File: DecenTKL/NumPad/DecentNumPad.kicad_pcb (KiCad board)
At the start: 2 copper layers, 78.6 x 146.7 mm, 129 parts, among them J1 Joystick1, J2 Joystick2, J3 Conn_02x20_Counter_Clockwise, J4 USB_A, J5 USB_C_Receptacle_USB2.0_16P, J6 USB_A, J7 USB_A, SW1 BOOTSEL, SW10 SW_Push, SW11 SW_Push, SW12 SW_Push, SW13 SW_Push, SW14 SW_Push, SW15 SW_Push, SW16 SW_Push, SW17 SW_Push, SW18 SW_Push, SW19 SW_Push, SW2 SW_Push, SW20 SW_Push, SW3 SW_Push, SW4 SW_Push, SW5 SW_Push, SW6 SW_Push, SW7 SW_Push, SW8 SW_Push, SW9 SW_Push, U1 NCP1117-3.3_SOT223, U2 W25Q128JVS, U3 RP2040, U4 CH334R, U5 CH213, Y1 ABM8-272-T3

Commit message: DecenTKL numpad update
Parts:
- added G***: LOGO, LOGO, F.Cu at (80.0, 19.0)
- added G***: LOGO, LOGO, B.Cu at (74.8, 159.6)
- added G***: LOGO, Library:ScreamingAtTheRadio, B.Cu at (93.8, 155.9)
- added REF**: KiCad-Logo2_6mm_Copper, Symbol:KiCad-Logo2_6mm_Copper, B.Cu at (50.3, 157.6)
- added REF**: OSHW-Logo2_7.3x6mm_Copper, Symbol:OSHW-Logo2_7.3x6mm_Copper, B.Cu at (40.1, 158.7)
- C1, C10, C11, C12, C13, C14, C15, C16, C17, C18, C19, C2, C3, C36, C37, C38, C4, C5, C6, C7, C8, C9: value 104 -> 100nF
- J5: footprint Connector_USB:USB_C_Receptacle_HRO_TYPE-C-31-M-12 -> Connector_USB:USB_C_Receptacle_HCTL_HC-TYPE-C-16P-01A
- SW17, SW8: footprint DecenTKL:Kailh_socket_MX_1-00U -> DecenTKL:Kailh_socket_MX_2-00U_V
- SW19: footprint DecenTKL:Kailh_socket_MX_1-00U -> DecenTKL:Kailh_socket_MX_2-00U
- moved C37 18.1 mm to (42.7, 142.3)
- moved C38 17.8 mm to (90.4, 132.8), turned to 90 degrees
- moved C36 16.7 mm to (90.3, 94.7)
- moved C18 14.6 mm to (27.5, 145.1)
- moved D41 14.3 mm to (94.6, 134.3)
- moved D39 14.3 mm to (94.6, 96.2)
- moved C4 9.74 mm to (51.2, 67.4), turned to 180 degrees
- moved D40 9.54 mm to (47.0, 143.8)
- moved C7 9.51 mm to (89.6, 83.3), turned to 180 degrees
- moved C16 9.50 mm to (89.6, 121.5), turned to 180 degrees
- moved C5 9.43 mm to (70.5, 66.9), turned to 180 degrees
- moved C6 9.38 mm to (89.6, 66.9), turned to 180 degrees
- moved C15 8.59 mm to (71.3, 123.3)
- moved C12 8.59 mm to (71.3, 104.2)
- moved C3 8.59 mm to (33.2, 66.0)
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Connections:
- D10 pad 1: /Minus/RGB_IN -> VBUS
- D10 pad 2: GND -> /Minus/RGB_IN
- D10 pad 3: /Over/RGB_OUT -> GND
- D10 pad 4: VBUS -> /Over/RGB_OUT
- D12 pad 1: /Minus/RGB_OUT -> VBUS
- D12 pad 2: GND -> /Minus/RGB_OUT
- D12 pad 3: /Minus/RGB_IN -> GND
- D12 pad 4: VBUS -> /Minus/RGB_IN
- D14 pad 1: /Four/RGB_IN -> VBUS
- D14 pad 2: GND -> /Four/RGB_IN
- D14 pad 3: /Nine/RGB_OUT -> GND
- D14 pad 4: VBUS -> /Nine/RGB_OUT
- D16 pad 1: /Eight/RGB_IN -> VBUS
- D16 pad 2: GND -> /Eight/RGB_IN
- D16 pad 3: /Minus/RGB_OUT -> GND
- D16 pad 4: VBUS -> /Minus/RGB_OUT
- D18 pad 1: /Eight/RGB_OUT -> VBUS
- D18 pad 2: GND -> /Eight/RGB_OUT
- D18 pad 3: /Eight/RGB_IN -> GND
- D18 pad 4: VBUS -> /Eight/RGB_IN
- D2 pad 1: /F11/RGB_OUT -> VBUS
- D2 pad 2: GND -> /F11/RGB_OUT
- D2 pad 3: RGB -> GND
- D2 pad 4: VBUS -> RGB
- D20 pad 1: /Nine/RGB_OUT -> VBUS
- D20 pad 2: GND -> /Nine/RGB_OUT
- D20 pad 3: /Eight/RGB_OUT -> GND
- D20 pad 4: VBUS -> /Eight/RGB_OUT
- D22 pad 1: /Five/RGB_OUT -> VBUS
- D22 pad 2: GND -> /Five/RGB_OUT
- D22 pad 3: /Five/RGB_IN -> GND
- D22 pad 4: VBUS -> /Five/RGB_IN
- D24 pad 1: /RGB44/RGB_IN -> VBUS
- D24 pad 2: GND -> /RGB44/RGB_IN
- D24 pad 3: /Five/RGB_OUT -> GND
- D24 pad 4: VBUS -> /Five/RGB_OUT
- D26 pad 1: /Three/RGB_IN -> VBUS
- D26 pad 2: GND -> /Three/RGB_IN
- D26 pad 3: /One/RGB_OUT -> GND
- D26 pad 4: VBUS -> /One/RGB_OUT
- D28 pad 1: /Five/RGB_IN -> VBUS
- D28 pad 2: GND -> /Five/RGB_IN
- D28 pad 3: /Four/RGB_IN -> GND
- D28 pad 4: VBUS -> /Four/RGB_IN
- D30 pad 1: /Enter/RGB_IN -> VBUS
- D30 pad 2: GND -> /Enter/RGB_IN
- D30 pad 3: /Three/RGB_IN -> GND
- D30 pad 4: VBUS -> /Three/RGB_IN
- D32 pad 1: /Enter/RGB_OUT -> VBUS
- D32 pad 2: GND -> /Enter/RGB_OUT
- D32 pad 3: /Enter/RGB_IN -> GND
- D32 pad 4: VBUS -> /Enter/RGB_IN
- D34 pad 1: /One/RGB_OUT -> VBUS
- D34 pad 2: GND -> /One/RGB_OUT
- D34 pad 3: /One/RGB_IN -> GND
- D34 pad 4: VBUS -> /One/RGB_IN
- D36 pad 1: /RGB62/RGB_IN -> VBUS
- D36 pad 2: GND -> /RGB62/RGB_IN
- D36 pad 3: /Enter/RGB_OUT -> GND
- D36 pad 4: VBUS -> /Enter/RGB_OUT
- D38 pad 1: /Point/RGB_OUT -> VBUS
- D38 pad 2: GND -> /Point/RGB_OUT
- D38 pad 3: /Point/RGB_IN -> GND
- D38 pad 4: VBUS -> /Point/RGB_IN
- D39 pad 1: /One/RGB_IN -> VBUS
- D39 pad 2: GND -> /One/RGB_IN
- D39 pad 3: /RGB44/RGB_IN -> GND
- D39 pad 4: VBUS -> /RGB44/RGB_IN
- D4 pad 1: /F12/RGB_OUT -> VBUS
- D4 pad 2: GND -> /F12/RGB_OUT
- D4 pad 3: /F11/RGB_OUT -> GND
- D4 pad 4: VBUS -> /F11/RGB_OUT
- D40 pad 1: /Point/RGB_IN -> VBUS
- D40 pad 2: GND -> /Point/RGB_IN
- D40 pad 3: /RGB62/RGB_IN -> GND
- D40 pad 4: VBUS -> /RGB62/RGB_IN
- D41 pad 1: /RGB63/RGB_OUT -> VBUS
- D41 pad 2: GND -> /RGB63/RGB_OUT
- D41 pad 3: /Point/RGB_OUT -> GND
- D41 pad 4: VBUS -> /Point/RGB_OUT
- D6 pad 1: /Num/RGB_OUT -> VBUS
- D6 pad 2: GND -> /Num/RGB_OUT
- D6 pad 3: /F12/RGB_OUT -> GND
- D6 pad 4: VBUS -> /F12/RGB_OUT
- D8 pad 1: /Over/RGB_OUT -> VBUS
- D8 pad 2: GND -> /Over/RGB_OUT
- D8 pad 3: /Num/RGB_OUT -> GND
- D8 pad 4: VBUS -> /Num/RGB_OUT
- J4 pad 5: unconnected-(J4-Shield-Pad5)_1 -> GND
- J5 pad S1: unconnected-(J5-SHIELD-PadS1)_1 -> GND
- J6 pad 5: unconnected-(J6-Shield-Pad5)_1 -> GND
- J7 pad 5: unconnected-(J7-Shield-Pad5)_1 -> GND
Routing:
- net VBUS: track 608.6 -> 709.9 mm
- net /Point/RGB_IN: track 14.1 -> 38.6 mm
- net GND: track 95.6 -> 119.7 mm, vias 96 -> 98
- net Net-(U5-VI+): track 23.0 -> 46.5 mm
- net /Point/RGB_OUT: track 14.8 -> 37.7 mm
- net /F12/RGB_OUT: track 97.9 -> 75.6 mm
- net /RGB44/RGB_IN: track 14.8 -> 37.0 mm
- net /F11/RGB_OUT: track 24.2 -> 44.6 mm
- net /Nine/RGB_OUT: track 14.1 -> 31.7 mm
- net /Enter/RGB_IN: track 14.1 -> 31.5 mm
- net /Minus/RGB_IN: track 14.1 -> 30.5 mm
- net /Num/RGB_OUT: track 14.1 -> 29.3 mm
- net /Over/RGB_OUT: track 14.1 -> 29.2 mm
- net /Eight/RGB_IN: track 14.1 -> 29.1 mm
- net /Five/RGB_IN: track 14.1 -> 29.0 mm
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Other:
- board size 78.6 x 146.7 mm -> 80.6 x 146.7 mm
- board text added: "*"
- board text added: "+"
- board text added: "-"
- board text added: "."
- board text added: "/"
- board text added: "0"
- board text added: "1"
- board text added: "2"
- board text added: "3"
- board text added: "3.3V"
- board text added: "4"
- board text added: "5"
- board text added: "6"
- board text added: "7"
- board text added: "8"
- board text added: "9"
- board text added: "Boot select"
- board text added: "COL0"
- board text added: "COL1"
- board text added: "COL2"
- board text added: "COL3"
- board text added: "DecenTKL numpad © Bertrand Le Roy 2024"
- board text added: "DecenTKL numpad © Bertrand Le Roy 2024 github.com/bleroy/3d-junkyard/DecenTKL"
- board text added: "Enter"
- board text added: "F11"
- board text added: "F12"
- board text added: "GND"
- board text added: "GP21"
- board text added: "GP22"
- board text added: "Joy 1"
- board text added: "Joy 2"
- board text added: "Joy1 down"
- board text added: "Joy1 left"
- board text added: "Joy1 right"
- board text added: "Joy1 trigger"
- board text added: "Joy1 up"
- board text added: "Joy2 down"
- board text added: "Joy2 left"
- board text added: "Joy2 right"
- board text added: "Joy2 trigger"
- board text added: "Joy2 up"
- board text added: "Num"
- board text added: "Paddle 2A"
- board text added: "Paddle 2B"
- board text added: "RGB"
- board text added: "ROW0"
- board text added: "ROW1"
- board text added: "ROW2"
- board text added: "ROW3"
- board text added: "ROW4"
- board text added: "ROW5"
- board text added: "USB 1"
- board text added: "USB 2"
- board text added: "USB 3"
- board text added: "USB in"

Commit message: DecenTKL NumPad WIP
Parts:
- SW10, SW11, SW12, SW13, SW14, SW15, SW16, SW17, SW18, SW19, SW2, SW20, SW3, SW4, SW5, SW6, SW7, SW8, SW9: value SW_Push -> MX
- moved J2 0.79 mm to (95.6, 42.1)
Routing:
- net JOY2_PADDLEA: track 106.5 -> 112.0 mm
- net JOY2_UP: track 73.1 -> 77.7 mm
- net JOY2_PADDLEB: track 94.7 -> 97.4 mm
- net JOY2_RIGHT: track 119.8 -> 121.4 mm
- net GP22: track 100.8 -> 102.0 mm
- net /2040/USB_BOOT: track 188.6 -> 189.6 mm
- net RGB: track 101.0 -> 102.0 mm
- net GP21: track 94.3 -> 95.2 mm
- net JOY2_LEFT: track 93.2 -> 94.1 mm
- net JOY2_DOWN: track 91.3 -> 90.5 mm
- net JOY2_TRIGGER: track 128.3 -> 129.0 mm
- net GND: track 119.7 -> 120.0 mm, vias 98 -> 100

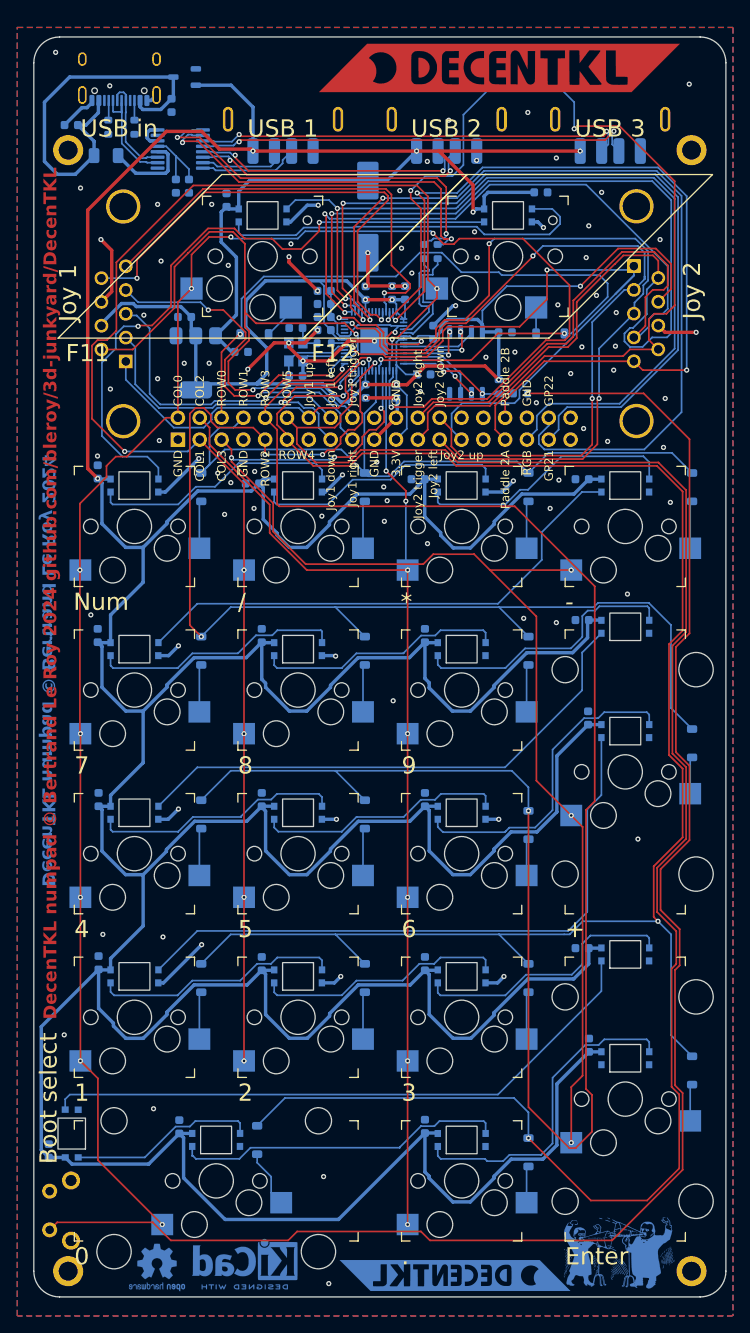
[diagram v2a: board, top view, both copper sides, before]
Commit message: DecenTKL NumPad rev. 1 finalized
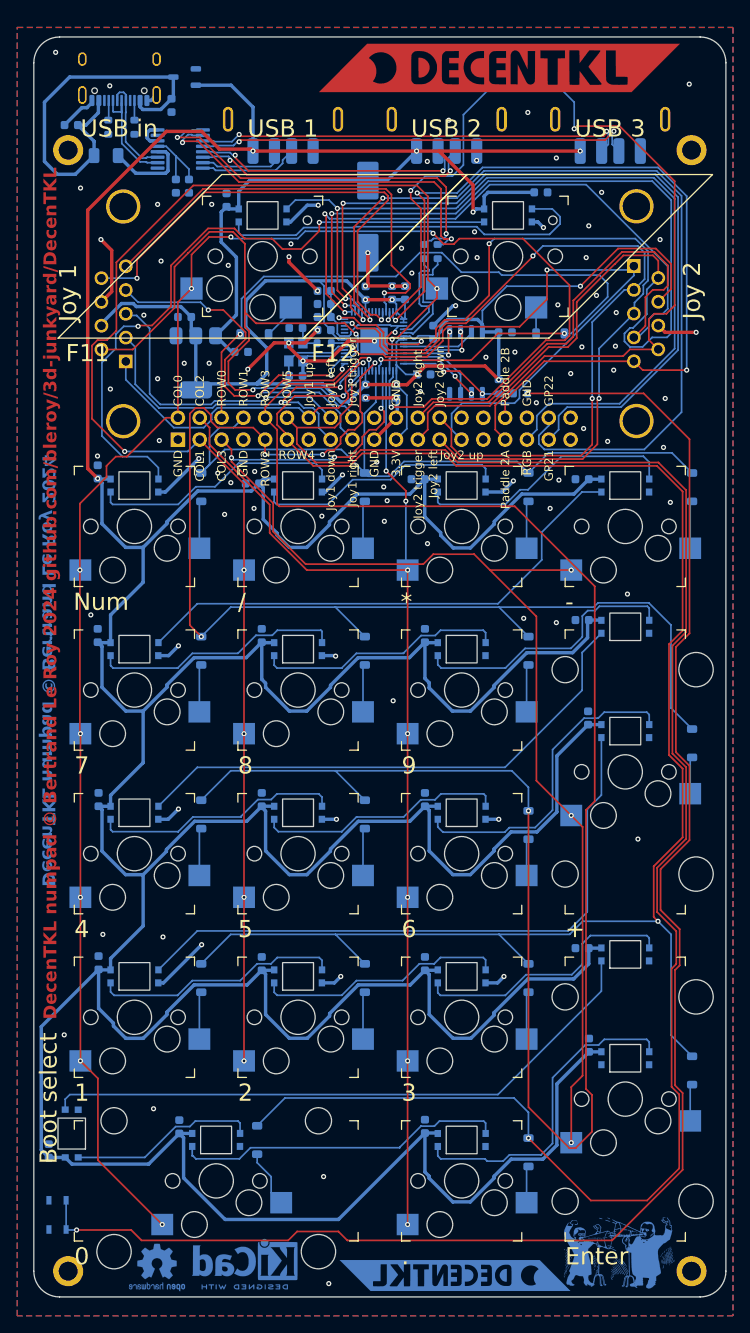
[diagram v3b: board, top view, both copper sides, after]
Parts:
- SW1: footprint Button_Switch_THT:SW_Tactile_SPST_Angled_PTS645Vx83-2LFS -> DecenTKL:SW_Push_1P1T_XKB_TS-1177A-C
- SW17, SW8: value MX -> 2UvMX
- SW19: value MX -> 2UMX
- SW2, SW3: value MX -> Choc
- moved SW1 2.91 mm to (28.5, 152.6)
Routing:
- net JOY2_UP: track 77.7 -> 74.0 mm
- net VBUS: track 709.9 -> 708.8 mm
- net JOY2_RIGHT: track 121.4 -> 120.3 mm
- net /2040/USB_BOOT: track 189.6 -> 190.3 mm, vias 1 -> 2
